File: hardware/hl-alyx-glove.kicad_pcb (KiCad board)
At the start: 2 copper layers, 85.6 x 41 mm, 38 parts, among them J1 OLED, J2 POWER, J3 IMU, J4 EXT_LED, SW1 SW_Push, SW2 SW_Push, U1 MAX7219, U2 MAX7219, U3 MAX7219, U4 ATmega328P-PU

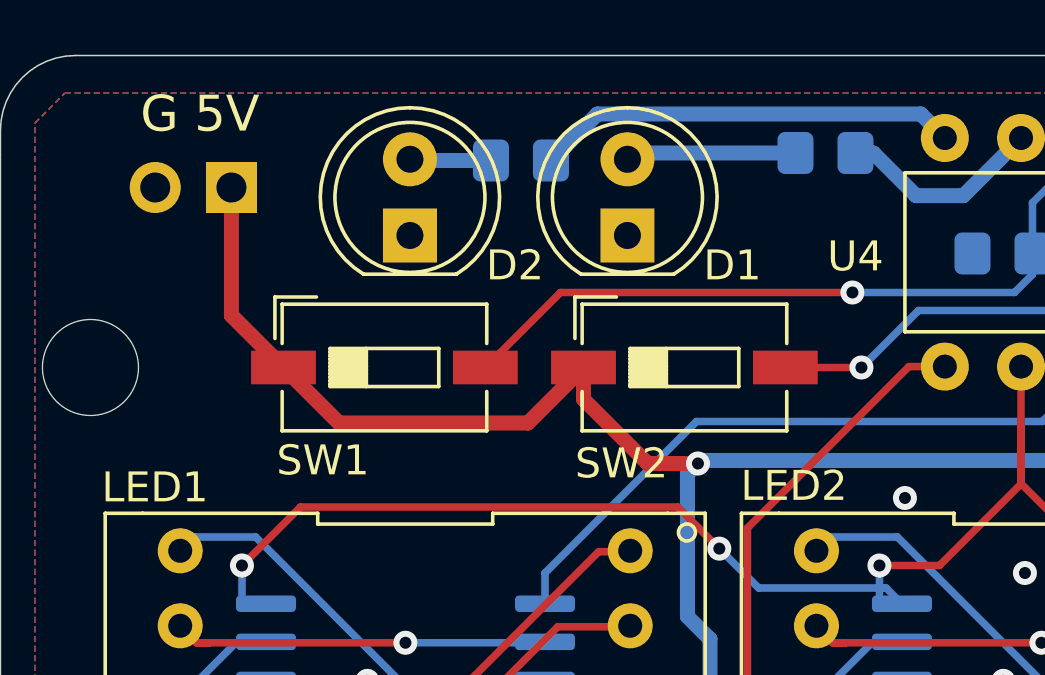
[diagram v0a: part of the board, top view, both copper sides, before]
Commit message: fix button footprints
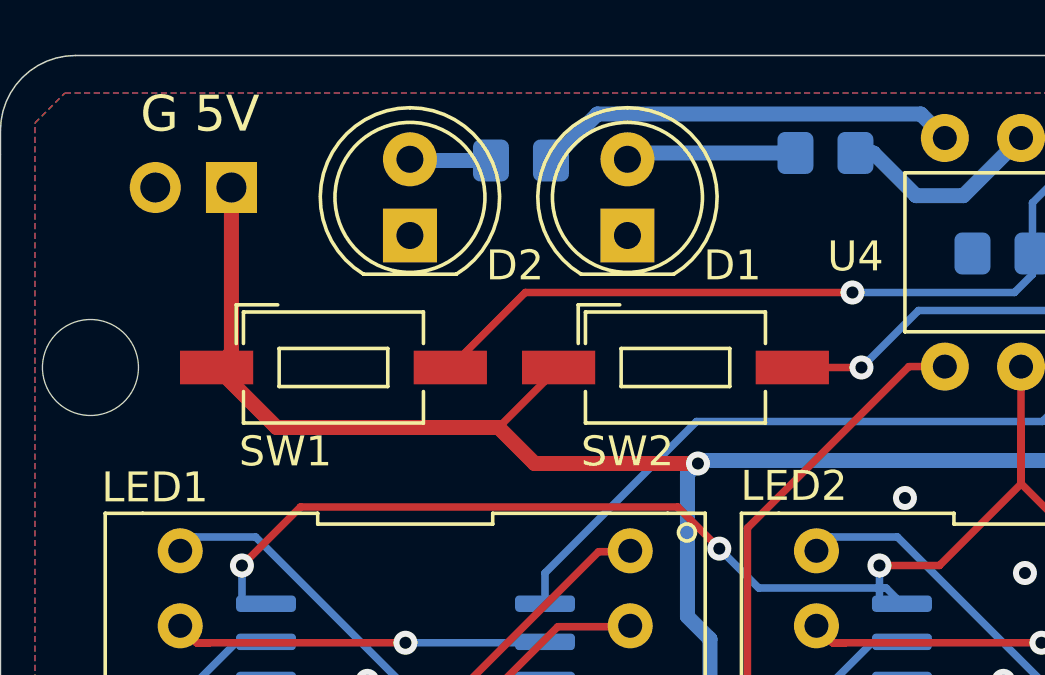
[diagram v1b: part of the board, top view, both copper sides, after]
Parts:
- SW1, SW2: footprint Button_Switch_SMD:SW_DIP_SPSTx01_Slide_6.7x4.1mm_W6.73mm_P2.54mm_LowProfile_JPin -> CustomComponents:smd_switch_sunrom4388
- moved SW1 1.70 mm to (97.2, 55.4)
- moved SW2 0.30 mm to (108.6, 55.4)
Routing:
- net Net-(R9-Pad2): track 25.0 -> 26.1 mm

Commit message: small fix
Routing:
- net VCC: track 210.9 -> 211.6 mm
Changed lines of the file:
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@@
     (thickness 1.6)
     (drawings 52)
-    (tracks 565)
+    (tracks 566)
     (zones 0)
     (modules 38)
@@
   (segment (start 117.65 83) (end 119.1 81.55) (width 0.25) (layer F.Cu) (net 74))
   (segment (start 109.5 83) (end 117.65 83) (width 0.25) (layer F.Cu) (net 74))
-  (segment (start 153 69.1) (end 153 70.25) (width 0.5) (layer B.Cu) (net 74))
-  (segment (start 155.1 67) (end 153 69.1) (width 0.5) (layer B.Cu) (net 74))
-  (segment (start 158.17 67) (end 155.1 67) (width 0.5) (layer B.Cu) (net 74))
-  (segment (start 159.97 68.8) (end 158.17 67) (width 0.5) (layer B.Cu) (net 74))
   (segment (start 109.45 58.5) (end 109.35 58.6) (width 0.5) (layer B.Cu) (net 74))
   (segment (start 127.15 58.5) (end 109.45 58.5) (width 0.5) (layer B.Cu) (net 74))
@@
   (segment (start 109.35 58.6) (end 103.905 58.6) (width 0.5) (layer F.Cu) (net 74))
   (segment (start 104.705 55.4) (end 102.705 57.4) (width 0.25) (layer F.Cu) (net 74))
+  (segment (start 155.5 66.6) (end 153 69.1) (width 0.5) (layer B.Cu) (net 74))
+  (segment (start 158.4 66.6) (end 155.5 66.6) (width 0.5) (layer B.Cu) (net 74))
+  (segment (start 159.97 68.17) (end 158.4 66.6) (width 0.5) (layer B.Cu) (net 74))
+  (segment (start 153 69.1) (end 153 70.25) (width 0.5) (layer B.Cu) (net 74))
+  (segment (start 159.97 68.8) (end 159.97 68.17) (width 0.5) (layer B.Cu) (net 74))
   (segment (start 143.779999 56.169999) (end 142.98 55.37) (width 0.25) (layer B.Cu) (net 75))
   (segment (start 145.035001 57.425001) (end 143.779999 56.169999) (width 0.25) (layer B.Cu) (net 75))
